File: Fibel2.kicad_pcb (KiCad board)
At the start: 2 copper layers, 210 x 148 mm, 274 parts, among them J1201 Orin Nano, J2 Bus_M.2_Socket_M, J301 Conn_01x02, J302 Conn_01x02, J303 Conn_01x02, J501 Conn_02x20_Odd_Even, J702 SPK_JST_L, J703 SPK_JST_R, J801 Conn_02x20_Odd_Even, Q301 CSD17581Q3A, Q302 CSD17581Q3A, Q303 CSD17581Q3A, Q304 CSD17581Q3A, U1 IT8951, U2 TPS651851RSLT, U201 TLV75718PDBV, U202 TLV75733PDBV, U203 TPS61022RWUR, U3 MX25L3206EM2I-12G, U301 BQ25798RQMR, U4 ESP32-S3-WROOM-1U, U402 TPS65988DHRSHR, U701 WM8960CGEFL

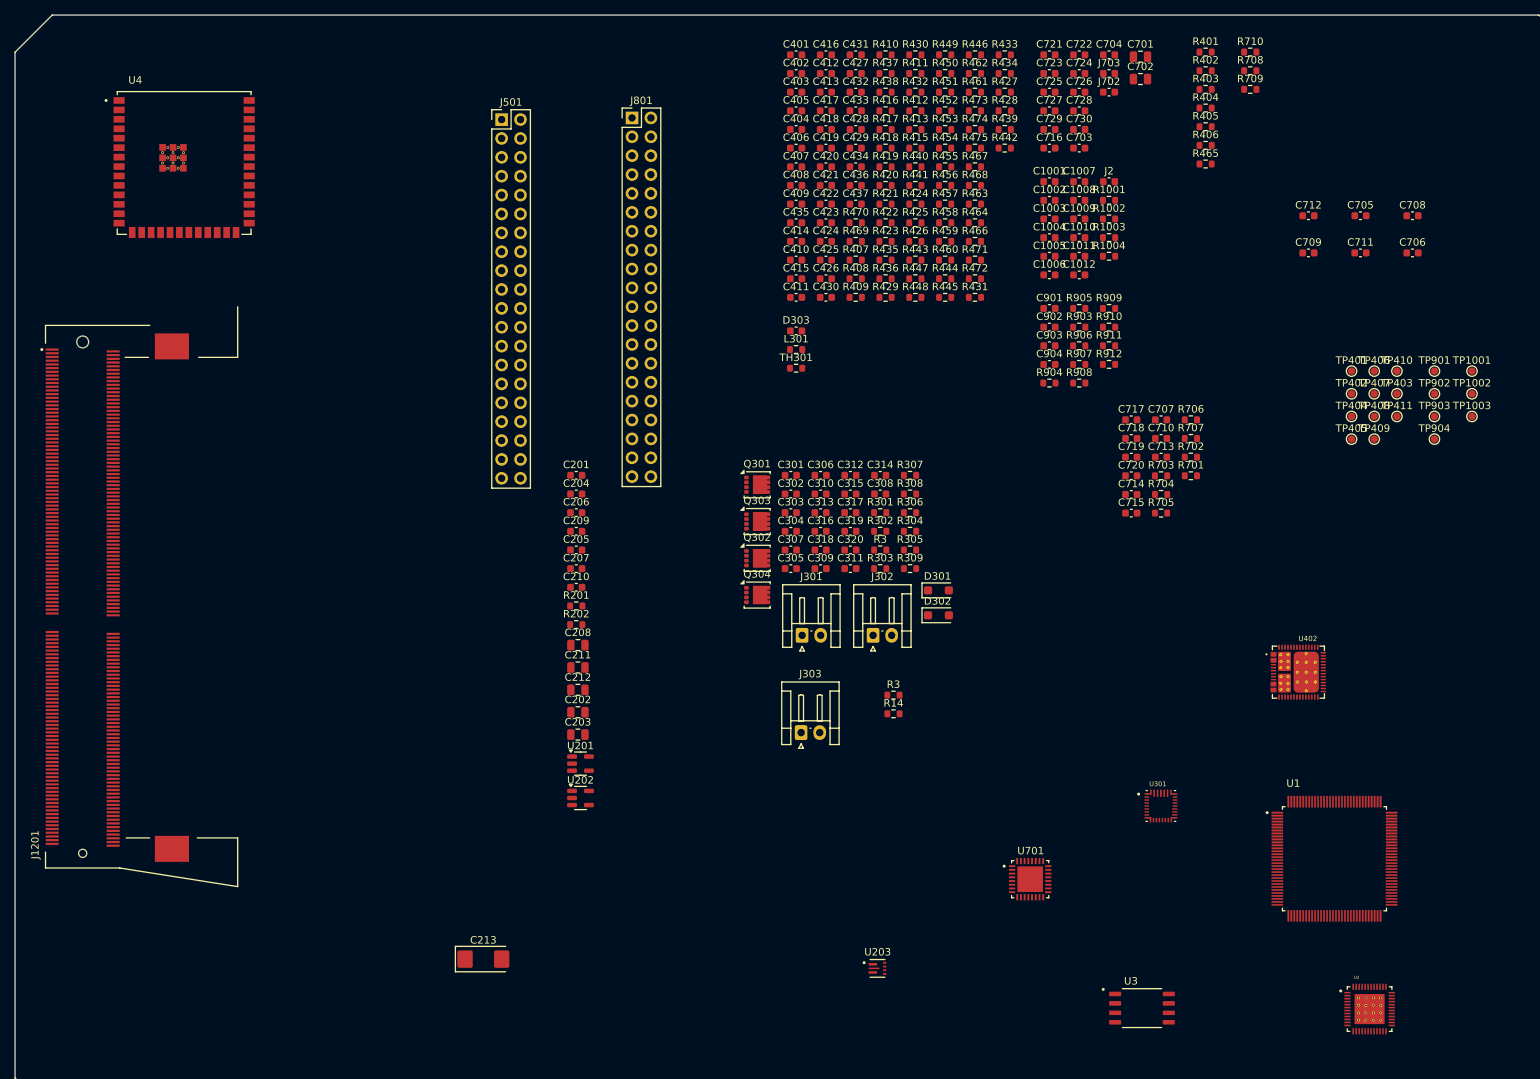
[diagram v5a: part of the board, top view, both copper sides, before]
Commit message: added connections to ESP32 S3, most oof EPD stuff that we're gooing to use is included
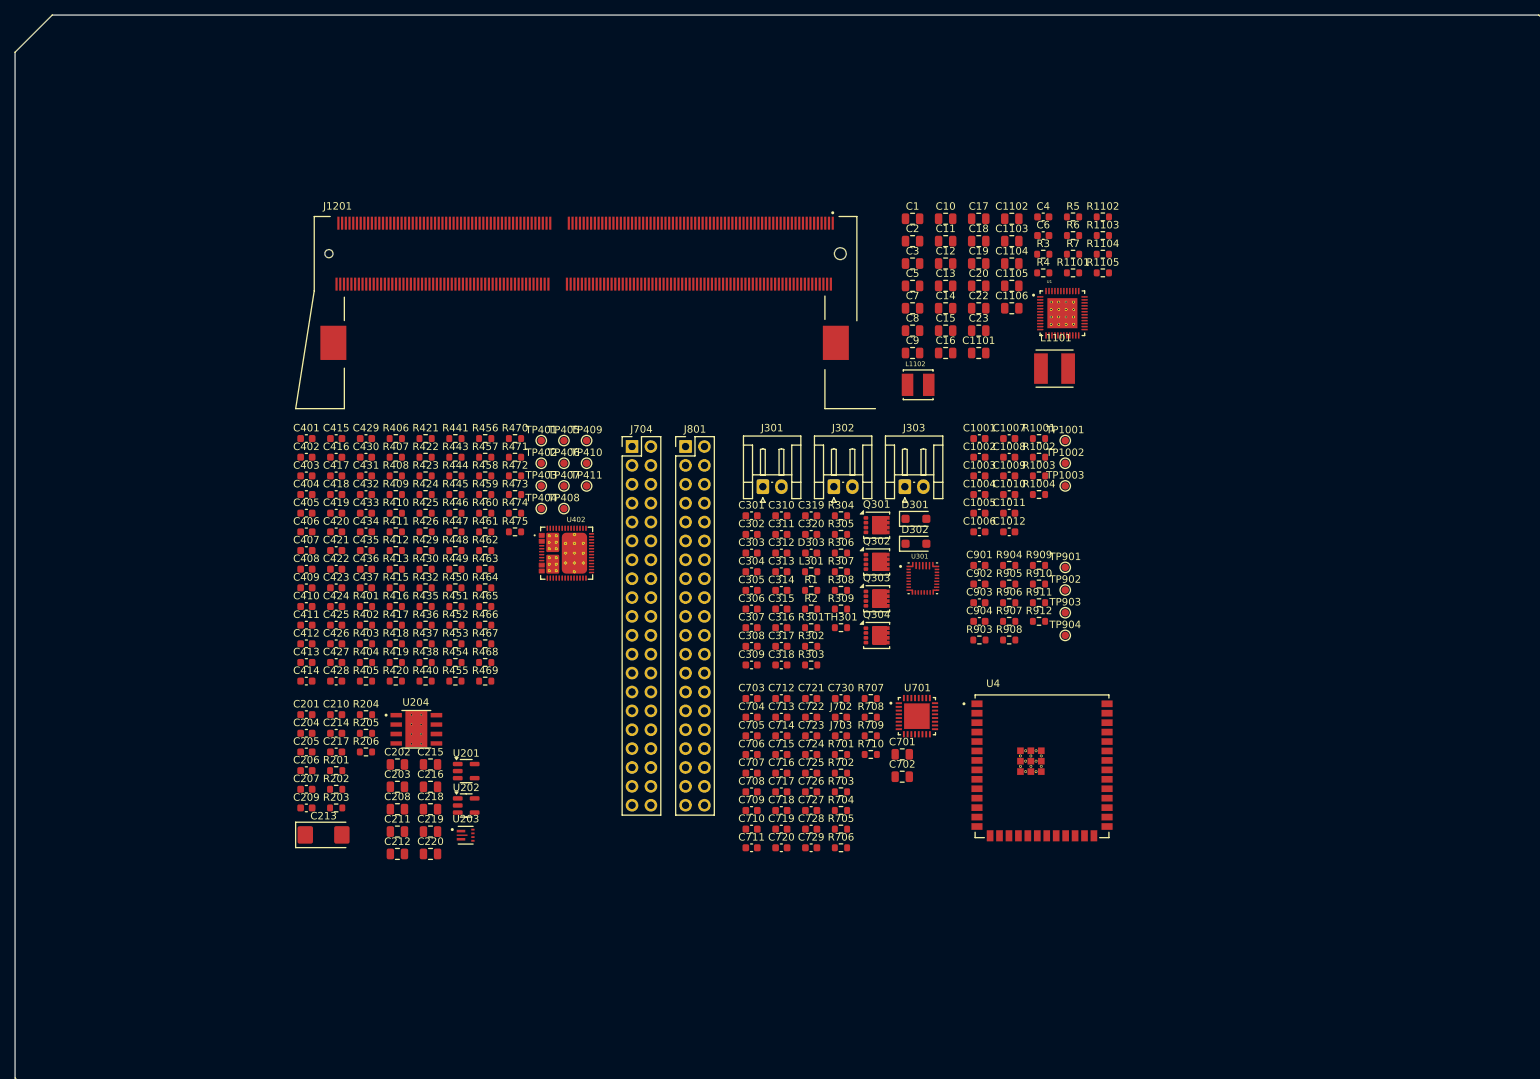
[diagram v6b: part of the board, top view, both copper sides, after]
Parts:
- removed J2: Bus_M.2_Socket_M, Capacitor_SMD:C_0603_1608Metric
- removed J501: Conn_02x20_Odd_Even, Connector_PinHeader_2.54mm:PinHeader_2x20_P2.54mm_Vertical
- removed R14: TBD/DNP, Resistor_SMD:R_0603_1608Metric
- removed the R3 at (133.2, 106.5)
- removed the R3 at (131.4, 87.0)
- removed R427, R428, R431, R433, R434, R439, R442: 0R, Resistor_SMD:R_0603_1608Metric
- removed U2: TPS651851RSLT, Fibel2:IC_TPS651851
- removed U3: MX25L3206EM2I-12G, Fibel2:SOIC127P790X216-8N
- added C1: 10nF, Capacitor_SMD:C_0805_2012Metric, F.Cu at (135.7, 42.4)
- added C10: 4.7uF, Capacitor_SMD:C_0805_2012Metric, F.Cu at (140.2, 42.4)
- added C11: 4.7uF, Capacitor_SMD:C_0805_2012Metric, F.Cu at (140.2, 45.4)
- added C1101: 10uF, Capacitor_SMD:C_0805_2012Metric, F.Cu at (144.6, 60.5)
- added C1102: 1uF, Capacitor_SMD:C_0805_2012Metric, F.Cu at (149.1, 42.4)
- added C1103: 1uF, Capacitor_SMD:C_0805_2012Metric, F.Cu at (149.1, 45.4)
- added C1104: 1uF, Capacitor_SMD:C_0805_2012Metric, F.Cu at (149.1, 48.4)
- added C1105: 1uF, Capacitor_SMD:C_0805_2012Metric, F.Cu at (149.1, 51.4)
- added C1106: 1uF, Capacitor_SMD:C_0805_2012Metric, F.Cu at (149.1, 54.4)
- added C12: 4.7uF, Capacitor_SMD:C_0805_2012Metric, F.Cu at (140.2, 48.4)
- added C13: 4.7uF, Capacitor_SMD:C_0805_2012Metric, F.Cu at (140.2, 51.4)
- added C14: 4.7uF, Capacitor_SMD:C_0805_2012Metric, F.Cu at (140.2, 54.4)
- added C15: 4.7uF, Capacitor_SMD:C_0805_2012Metric, F.Cu at (140.2, 57.5)
- added C16: 4.7uF, Capacitor_SMD:C_0805_2012Metric, F.Cu at (140.2, 60.5)
- added C17: 10nF, Capacitor_SMD:C_0805_2012Metric, F.Cu at (144.6, 42.4)
- added C18: 10nF, Capacitor_SMD:C_0805_2012Metric, F.Cu at (144.6, 45.4)
- added C19: 4.7uF, Capacitor_SMD:C_0805_2012Metric, F.Cu at (144.6, 48.4)
- added C2: 100nF, Capacitor_SMD:C_0805_2012Metric, F.Cu at (135.7, 45.4)
- added C20: 100nF, Capacitor_SMD:C_0805_2012Metric, F.Cu at (144.6, 51.4)
- added C214: 10uF, Capacitor_SMD:C_0603_1608Metric, F.Cu at (58.2, 111.6)
- added C215: 22uF, Capacitor_SMD:C_0805_2012Metric, F.Cu at (70.9, 115.8)
- added C216: 22uF, Capacitor_SMD:C_0805_2012Metric, F.Cu at (70.9, 118.8)
- added C217: 22uF, Capacitor_SMD:C_0603_1608Metric, F.Cu at (58.2, 114.1)
- added C218: 22uF, Capacitor_SMD:C_0805_2012Metric, F.Cu at (70.9, 121.8)
- added C219: 22uF, Capacitor_SMD:C_0805_2012Metric, F.Cu at (70.9, 124.8)
- added C22: 2.2uF, Capacitor_SMD:C_0805_2012Metric, F.Cu at (144.6, 54.4)
- added C220: 0.1uF, Capacitor_SMD:C_0805_2012Metric, F.Cu at (70.9, 127.9)
- added C23: 10uF, Capacitor_SMD:C_0805_2012Metric, F.Cu at (144.6, 57.5)
- added C3: 22uF, Capacitor_SMD:C_0805_2012Metric, F.Cu at (135.7, 48.4)
- added C4: 10uF, Capacitor_SMD:C_0603_1608Metric, F.Cu at (153.3, 42.2)
- added C5: 22uF, Capacitor_SMD:C_0805_2012Metric, F.Cu at (135.7, 51.4)
- added C6: 10uF, Capacitor_SMD:C_0603_1608Metric, F.Cu at (153.3, 44.7)
- added C7: 4.7uF, Capacitor_SMD:C_0805_2012Metric, F.Cu at (135.7, 54.4)
- added C8: 4.7uF, Capacitor_SMD:C_0805_2012Metric, F.Cu at (135.7, 57.5)
- added C9: 4.7uF, Capacitor_SMD:C_0805_2012Metric, F.Cu at (135.7, 60.5)
- added J704: Conn_02x20_Odd_Even, Connector_PinHeader_2.54mm:PinHeader_2x20_P2.54mm_Vertical, F.Cu at (98.0, 73.0)
- added L1101: 4.7uH, Fibel2:IND_LQH5BPB4R7NT0L, F.Cu at (154.8, 62.6)
- added L1102: 2.2uH, Fibel2:IND_LQH44PN4R7MP0L, F.Cu at (136.5, 64.7)
- added R1: 0R, Resistor_SMD:R_0603_1608Metric, F.Cu at (122.1, 92.4)
- added R1101: 47K, Resistor_SMD:R_0603_1608Metric, F.Cu at (157.3, 49.7)
- added R1102: 47K, Resistor_SMD:R_0603_1608Metric, F.Cu at (161.3, 42.2)
- added R1103: 47K, Resistor_SMD:R_0603_1608Metric, F.Cu at (161.3, 44.7)
- added R1104: 47K, Resistor_SMD:R_0603_1608Metric, F.Cu at (161.3, 47.2)
- added R1105: 100K, Resistor_SMD:R_0603_1608Metric, F.Cu at (161.3, 49.7)
- added R2: 0R, Resistor_SMD:R_0603_1608Metric, F.Cu at (122.1, 94.9)
- added R203: 10K, Resistor_SMD:R_0603_1608Metric, F.Cu at (58.2, 121.7)
- added R204: 49.9K, Resistor_SMD:R_0603_1608Metric, F.Cu at (62.2, 109.1)
- added R205: 365K, Resistor_SMD:R_0603_1608Metric, F.Cu at (62.2, 111.6)
- added R206: 100K, Resistor_SMD:R_0603_1608Metric, F.Cu at (62.2, 114.1)
- added R3: 1M, Resistor_SMD:R_0603_1608Metric, F.Cu at (153.3, 47.2)
- added R4: 52.3K, Resistor_SMD:R_0603_1608Metric, F.Cu at (153.3, 49.7)
- added R5: 1M, Resistor_SMD:R_0603_1608Metric, F.Cu at (157.3, 42.2)
- added R6: 47.5K, Resistor_SMD:R_0603_1608Metric, F.Cu at (157.3, 44.7)
- added R7: 0R, Resistor_SMD:R_0603_1608Metric, F.Cu at (157.3, 47.2)
- added U204: TPS56428DDA, Fibel2:TPS56428DDA, F.Cu at (69.0, 111.1)
- U1: value IT8951 -> TPS651851RSLT; footprint Fibel2:QFP40P1600X1600X160-128N -> Fibel2:IC_TPS651851
- moved U4 141.1 mm to (153.2, 116.1)
- moved R402 135.4 mm to (62.2, 97.1)
- moved R405 135.4 mm to (62.2, 104.6)
- moved R401 135.4 mm to (62.2, 94.6)
- moved R403 135.4 mm to (62.2, 99.6)
- moved R404 135.4 mm to (62.2, 102.1)
- moved C708 117.9 mm to (114.1, 119.5)
- moved R406 115.9 mm to (66.2, 72.0)
- moved TP403 115.8 mm to (85.8, 78.3)
- moved C711 114.5 mm to (114.1, 127.0)
- moved R465 113.7 mm to (78.3, 94.6)
- moved C706 111.6 mm to (114.1, 114.5)
- moved TP404 109.7 mm to (85.8, 81.4)
- moved TP410 109.7 mm to (91.9, 75.3)
- moved TP406 109.7 mm to (88.8, 75.3)
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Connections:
- net GPIO01 renamed RP_GPIO05
- net GPIO07 renamed RP_GPIO12
- net GPIO09 renamed RP_GPIO04
- net GPIO11 renamed RP_GPIO06
- net GPIO12 renamed RP_GPIO22
- net GPIO13 renamed RP_GPIO13
- J1201 pad 232: unconnected-(J1201D-I2C2_SCL-Pad232) -> I2C1_SCL
- J1201 pad 234: unconnected-(J1201D-I2C2_SDA-Pad234) -> I2C1_SDA
- J1201 pad 251: Net-(J1201D-VDD_IN-Pad251) -> VDD_MOD
- J1201 pad 252: Net-(J1201D-VDD_IN-Pad252) -> VDD_MOD
- J1201 pad 253: Net-(J1201D-VDD_IN-Pad251) -> VDD_MOD
- J1201 pad 254: Net-(J1201D-VDD_IN-Pad252) -> VDD_MOD
- J1201 pad 255: Net-(J1201D-VDD_IN-Pad251) -> VDD_MOD
- J1201 pad 256: Net-(J1201D-VDD_IN-Pad252) -> VDD_MOD
- J1201 pad 257: Net-(J1201D-VDD_IN-Pad251) -> VDD_MOD
- J1201 pad 258: Net-(J1201D-VDD_IN-Pad252) -> VDD_MOD
- J1201 pad 259: Net-(J1201D-VDD_IN-Pad251) -> VDD_MOD
- J1201 pad 260: Net-(J1201D-VDD_IN-Pad252) -> VDD_MOD
- J1201 pad 89: unconnected-(J1201B-SPI0_MOSI-Pad89) -> SPI0_MOSI
- J1201 pad 91: unconnected-(J1201B-SPI0_SCK-Pad91) -> SPI0_SCK
- J1201 pad 93: unconnected-(J1201B-SPI0_MISO-Pad93) -> SPI0_MISO
- J1201 pad 95: unconnected-(J1201B-SPI0_CS0-Pad95) -> SPI0_CS0
- J1201 pad 97: unconnected-(J1201B-SPI0_CS1-Pad97) -> SPI0_CS1
- J801 pad 11: unconnected-(J801-Pin_11-Pad11) -> RP_GPIO17
- J801 pad 13: unconnected-(J801-Pin_13-Pad13) -> RP_GPIO27
- J801 pad 16: unconnected-(J801-Pin_16-Pad16) -> RP_GPIO23
- J801 pad 18: unconnected-(J801-Pin_18-Pad18) -> RP_GPIO24
- J801 pad 22: unconnected-(J801-Pin_22-Pad22) -> RP_GPIO25
- J801 pad 27: unconnected-(J801-Pin_27-Pad27) -> RP_ID_SD
- J801 pad 28: unconnected-(J801-Pin_28-Pad28) -> RP_ID_SC
- J801 pad 36: unconnected-(J801-Pin_36-Pad36) -> RP_GPIO16
- J801 pad 37: unconnected-(J801-Pin_37-Pad37) -> RP_GPIO26
- U1 pad 1: unconnected-(U1-VCCK-Pad1) -> Net-(U1-VREF)
- U1 pad 10: unconnected-(U1-HOST_HRD_N-Pad10) -> EPD_VIN
- U1 pad 12: unconnected-(U1-HOST_HD_C/SPI_SI-Pad12) -> /EPD/EPD_VCOM_CTRL
- U1 pad 14: unconnected-(U1-HOST_HIRQ-Pad14) -> GND
- U1 pad 15: unconnected-(U1-HOST_HDB0/SPI_SCK-Pad15) -> /EPD/EPD_VCOM
- U1 pad 16: unconnected-(U1-HOST_HDB1/SPI_CS_N-Pad16) -> /EPD/EPD_VNEG_IN
- U1 pad 17: unconnected-(U1-HOST_HDB2/SPI_SO-Pad17) -> /EPD/EPD_SCL
- U1 pad 18: unconnected-(U1-HOST_HDB3-Pad18) -> /EPD/EPD_SDA
- U1 pad 19: unconnected-(U1-HOST_HDB4-Pad19) -> 15V
- U1 pad 2: unconnected-(U1-RESET_N-Pad2) -> /EPD/~{EPD_INT}
- U1 pad 21: unconnected-(U1-GND-Pad21) -> /EPD/EPD_PWRUP
- U1 pad 22: unconnected-(U1-HOST_HDB5-Pad22) -> /EPD/EPD_VNEG_IN
- U1 pad 23: unconnected-(U1-HOST_HDB6-Pad23) -> /EPD/EPD_PWRGD
- U1 pad 24: unconnected-(U1-HOST_HDB7-Pad24) -> EPD_VIN
- U1 pad 25: unconnected-(U1-HOST_HDB8-Pad25) -> Net-(U1-VN_SW)
- U1 pad 26: unconnected-(U1-HOST_HDB9-Pad26) -> /EPD/EPD_VNEG_IN
- U1 pad 27: unconnected-(U1-HOST_HDB10-Pad27) -> /EPD/EPD_VNEG_IN
- U1 pad 28: unconnected-(U1-HOST_HDB11-Pad28) -> Net-(U1-VEE_DRV)
- U1 pad 29: unconnected-(U1-HOST_HDB12-Pad29) -> -20V
- U1 pad 3: unconnected-(U1-TEST_EN-Pad3) -> -15V
- U1 pad 30: unconnected-(U1-HOST_HDB13-Pad30) -> Net-(U1-VEE_D)
- U1 pad 31: unconnected-(U1-HOST_HDB14-Pad31) -> Net-(U1-VEE_FB)
- U1 pad 32: unconnected-(U1-HOST_HDB15-Pad32) -> GND
- U1 pad 33: unconnected-(U1-VCC33A-Pad33) -> Net-(U1-VDDH_FB)
- U1 pad 34: unconnected-(U1-VREF-Pad34) -> Net-(U1-VDDH_D)
- U1 pad 35: unconnected-(U1-TS_EX-Pad35) -> +22V
- U1 pad 36: unconnected-(U1-DN-Pad36) -> Net-(U1-VDDH_DRV)
- U1 pad 37: unconnected-(U1-GNDA-Pad37) -> /EPD/EPD_VPOS_IN
- U1 pad 4: unconnected-(U1-TEST_CFG0-Pad4) -> /EPD/EPD_VNEG_IN
- U1 pad 40: unconnected-(U1-NC-Pad40) -> /EPD/EPD_VB_SW
- U1 pad 41: unconnected-(U1-NC-Pad41) -> GND
- U1 pad 42: unconnected-(U1-D-Pad42) -> /EPD/EPD_VPOS_IN
- U1 pad 43: unconnected-(U1-NC-Pad43) -> /EPD/EPD_VPOS_IN
- U1 pad 44: unconnected-(U1-NC-Pad44) -> 15V
- U1 pad 45: unconnected-(U1-VS33D-Pad45) -> EPD_3V3
- U1 pad 46: unconnected-(U1-XSCI-Pad46) -> /EPD/EPD_VDD
- U1 pad 48: unconnected-(U1-VCC33A_HSRT-Pad48) -> GND
- U1 pad 49: unconnected-(U1-GND33A_HSRT-Pad49) -> (no net)
- U1 pad 5: unconnected-(U1-TEST_CFG1-Pad5) -> /EPD/EPD_WAKE
- U1 pad 50: unconnected-(U1-RREF-Pad50) -> (no net)
- U1 pad 51: unconnected-(U1-DM-Pad51) -> (no net)
- U1 pad 52: unconnected-(U1-DP-Pad52) -> (no net)
- U1 pad 53: unconnected-(U1-VCC33A_U20-Pad53) -> (no net)
- U1 pad 54: unconnected-(U1-GND33A_U20-Pad54) -> (no net)
- U1 pad 55: unconnected-(U1-VCCK-Pad55) -> (no net)
- U1 pad 56: unconnected-(U1-PWR_S_P/VCOM[0]-Pad56) -> (no net)
- U1 pad 57: unconnected-(U1-PWR_S_N/VCOM[1]-Pad57) -> (no net)
- U1 pad 58: unconnected-(U1-PWR_G_P/VCOM1[0]-Pad58) -> (no net)
- U1 pad 59: unconnected-(U1-PWR_G_N/VCOM1[1]-Pad59) -> (no net)
- U1 pad 6: unconnected-(U1-TEST_CFG2-Pad6) -> GND
- U1 pad 60: unconnected-(U1-VCC3IO-Pad60) -> (no net)
- U1 pad 61: unconnected-(U1-GND-Pad61) -> (no net)
- U1 pad 62: unconnected-(U1-GPIO8/PWR[0]-Pad62) -> (no net)
- U1 pad 63: unconnected-(U1-GPIO9/PWR[1]-Pad63) -> (no net)
- U1 pad 64: unconnected-(U1-GPIO10/PWR[2]-Pad64) -> (no net)
- U1 pad 65: unconnected-(U1-GPIO11/PWR[3]-Pad65) -> (no net)
- U1 pad 7: unconnected-(U1-UART_TX-Pad7) -> Net-(U1-INT_LDO)
- U1 pad 8: unconnected-(U1-UART_RX-Pad8) -> GND
- U1 pad 9: unconnected-(U1-HOST_HWE_N-Pad9) -> -15V
